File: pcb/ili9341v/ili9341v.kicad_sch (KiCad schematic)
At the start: 6 parts, among them J2 Conn_01x14_Socket

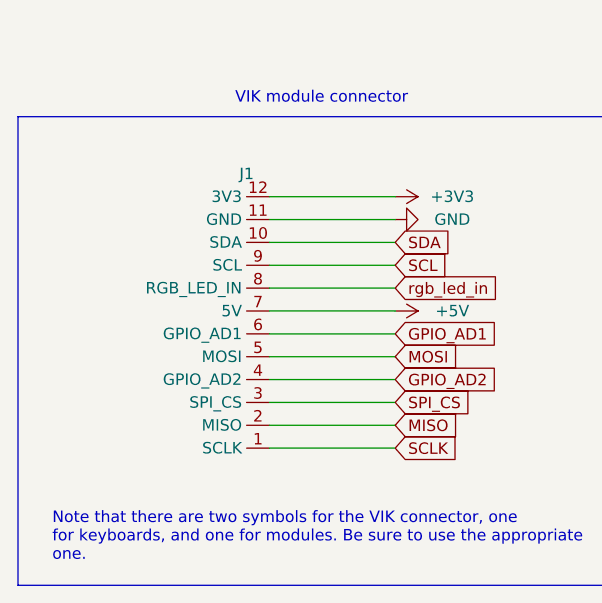
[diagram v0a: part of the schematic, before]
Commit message: updated vikm connector symbols, per some recommendations from sigprof in fingerpunch discord
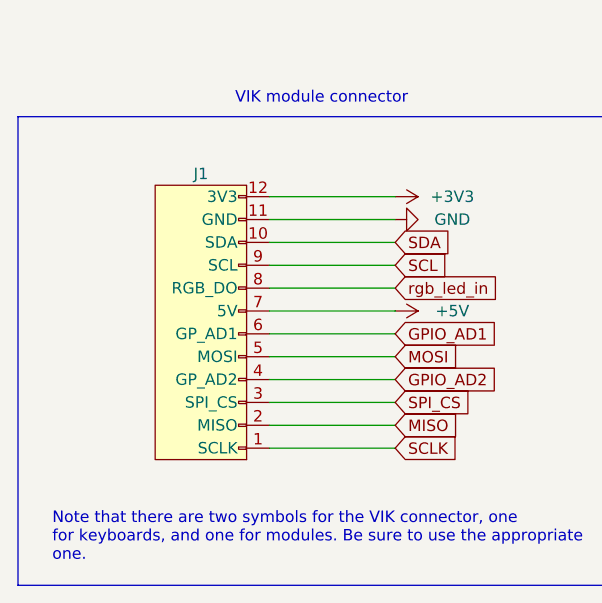
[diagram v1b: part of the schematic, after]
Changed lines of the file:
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@@
     )
   )
-  (symbol (lib_id "vik:vik-module-connector") (at 81.28 72.39 180) (unit 1)
-    (in_bom yes) (on_board yes) (dnp no) (fields_autoplaced)
-    (property "Reference" "J1" (at 78.74 55.88 0)
+  (symbol (lib_id "vik:vik-module-connector") (at 73.66 73.66 180) (unit 1)
+    (in_bom yes) (on_board yes) (dnp no)
+    (property "Reference" "J1" (at 73.66 55.88 0)
       (effects (font (size 1.27 1.27)))
     )
-    (property "Value" "~" (at 81.28 78.74 0)
+    (property "Value" "~" (at 73.66 80.01 0)
       (effects (font (size 1.27 1.27)))
     )
-    (property "Footprint" "vik:vik-module-connector-horizontal" (at 81.28 78.74 0)
+    (property "Footprint" "vik:vik-module-connector-horizontal" (at 73.66 80.01 0)
       (effects (font (size 1.27 1.27)) hide)
     )
-    (property "Datasheet" "" (at 81.28 78.74 0)
+    (property "Datasheet" "" (at 73.66 80.01 0)
       (effects (font (size 1.27 1.27)) hide)
     )
-    (property "LCSC" "C479750" (at 81.28 72.39 0)
+    (property "LCSC" "C479750" (at 73.66 73.66 0)
       (effects (font (size 1.27 1.27)) hide)
     )

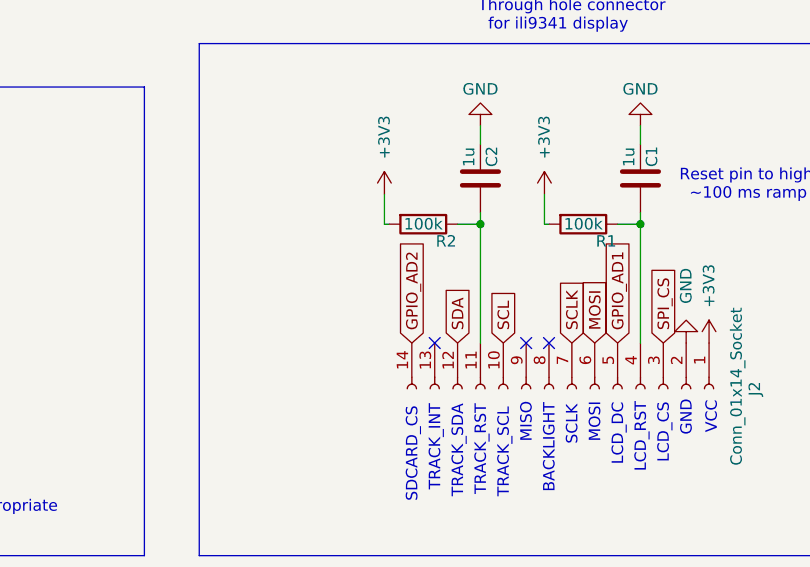
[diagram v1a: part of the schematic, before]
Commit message: added MISO for SD card support, added jumper to select between backlight and sd card, defaults to backlight
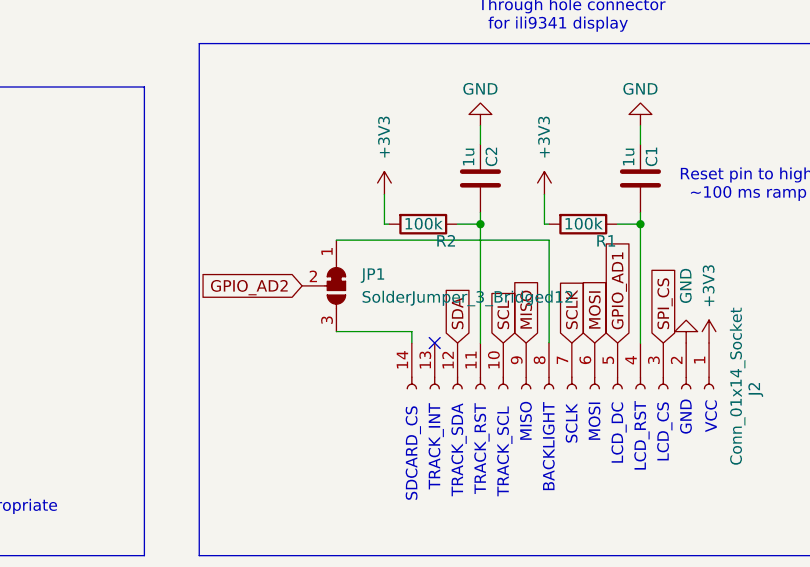
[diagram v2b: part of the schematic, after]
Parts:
- added JP1: SolderJumper_3_Bridged12, Jumper:SolderJumper-3_P1.3mm_Bridged12_RoundedPad1.0x1.5mm_NumberLabels, symbol Jumper:SolderJumper_3_Bridged12
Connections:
- net GPIO_AD2: now also JP1.2 (C); no longer J2.14 (Pin_14)
- net MISO: now also J2.9 (Pin_9)
- net at J2.8 (Pin_8): now also JP1.1 (A)
- new net: J2.14 (Pin_14), JP1.3 (B)
- no-connect marks 3 -> 1
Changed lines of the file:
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@@
   (junction (at 163.068 64.77) (diameter 0) (color 0 0 0 0)
   )
-  (no_connect (at 168.148 77.978))
   (no_connect (at 157.988 77.978))
-  (no_connect (at 170.688 77.978))
+  (wire (pts (xy 170.688 66.548) (xy 170.688 77.978))
+    (stroke (width 0) (type default))
+  )
   (wire (pts (xy 81.28 58.42) (xy 95.25 58.42))
     (stroke (width 0) (type default))
@@
     (stroke (width 0) (type default))
   )
+  (wire (pts (xy 147.066 66.548) (xy 170.688 66.548))
+    (stroke (width 0) (type default))
+  )
   (wire (pts (xy 163.068 53.848) (xy 163.068 55.88))
     (stroke (width 0) (type default))
@@
   )
   (wire (pts (xy 81.28 68.58) (xy 95.25 68.58))
+    (stroke (width 0) (type default))
+  )
+  (wire (pts (xy 155.448 76.708) (xy 155.448 77.978))
+    (stroke (width 0) (type default))
+  )
+  (wire (pts (xy 147.066 76.708) (xy 155.448 76.708))
     (stroke (width 0) (type default))
   )
@@
     (effects (font (size 1.27 1.27)) (justify left bottom))
   )
+  (global_label "MISO" (shape input) (at 168.148 77.978 90) (fields_autoplaced)
+    (effects (font (size 1.27 1.27)) (justify left))
+    (property "Intersheetrefs" "${INTERSHEET_REFS}" (at 168.148 71.1302 90)
+      (effects (font (size 1.27 1.27)) (justify left) hide)
+    )
+  )
   (global_label "GPIO_AD1" (shape input) (at 178.308 77.978 90) (fields_autoplaced)
     (effects (font (size 1.27 1.27)) (justify left))
@@
     )
   )
-  (global_label "GPIO_AD2" (shape input) (at 155.448 77.978 90) (fields_autoplaced)
-    (effects (font (size 1.27 1.27)) (justify left))
-    (property "Intersheetrefs" "${INTERSHEET_REFS}" (at 155.448 66.7154 90)
-      (effects (font (size 1.27 1.27)) (justify left) hide)
+  (global_label "GPIO_AD2" (shape input) (at 143.256 71.628 180) (fields_autoplaced)
+    (effects (font (size 1.27 1.27)) (justify right))
+    (property "Intersheetrefs" "${INTERSHEET_REFS}" (at 131.9934 71.628 0)
+      (effects (font (size 1.27 1.27)) (justify right) hide)
     )
   )
@@
         )
       )
+    )
+  )
+  (symbol (lib_id "Jumper:SolderJumper_3_Bridged12") (at 147.066 71.628 270) (unit 1)
+    (in_bom yes) (on_board yes) (dnp no) (fields_autoplaced)
+    (property "Reference" "JP1" (at 149.86 70.358 90)
+      (effects (font (size 1.27 1.27)) (justify left))
+    )
+    (property "Value" "SolderJumper_3_Bridged12" (at 149.86 72.898 90)
+      (effects (font (size 1.27 1.27)) (justify left))
+    )
+    (property "Footprint" "Jumper:SolderJumper-3_P1.3mm_Bridged12_RoundedPad1.0x1.5mm_NumberLabels" (at 147.066 71.628 0)
+      (effects (font (size 1.27 1.27)) hide)
+    )
+    (property "Datasheet" "~" (at 147.066 71.628 0)
+      (effects (font (size 1.27 1.27)) hide)
+    )
+    (pin "1")
+    (pin "2")
+    (pin "3")
+    (instances
+      (project "ili9341v"
+        (path "/61fe293f-6808-4b7f-9340-9aaac7054a97"
+          (reference "JP1") (unit 1)
+        )
+      )

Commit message: ili9341v display module - updated to use hand solderable capacitors, 1206 instead of 0402
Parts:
- C1, C2: footprint Capacitor_SMD:C_0402_1005Metric -> Capacitor_SMD:C_1206_3216Metric_Pad1.33x1.80mm_HandSolder; LCSC C52923 -> C90539
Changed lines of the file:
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@@
       (effects (font (size 1.27 1.27)) (justify left))
     )
-    (property "Footprint" "Capacitor_SMD:C_0402_1005Metric" (at 179.8828 63.5 0)
+    (property "Footprint" "Capacitor_SMD:C_1206_3216Metric_Pad1.33x1.80mm_HandSolder" (at 179.8828 63.5 0)
       (effects (font (size 1.27 1.27)) hide)
     )
@@
       (effects (font (size 1.27 1.27)) hide)
     )
-    (property "LCSC" "C52923" (at 180.848 59.69 0)
+    (property "LCSC" "C90539" (at 180.848 59.69 0)
       (effects (font (size 1.27 1.27)) hide)
     )
@@
       (effects (font (size 1.27 1.27)) (justify left))
     )
-    (property "Footprint" "Capacitor_SMD:C_0402_1005Metric" (at 162.1028 63.5 0)
+    (property "Footprint" "Capacitor_SMD:C_1206_3216Metric_Pad1.33x1.80mm_HandSolder" (at 162.1028 63.5 0)
       (effects (font (size 1.27 1.27)) hide)
     )
@@
       (effects (font (size 1.27 1.27)) hide)
     )
-    (property "LCSC" "C52923" (at 163.068 59.69 0)
+    (property "LCSC" "C90539" (at 163.068 59.69 0)
       (effects (font (size 1.27 1.27)) hide)
     )
